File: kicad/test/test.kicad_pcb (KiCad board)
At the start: 2 copper layers, 100.3 x 46.4 mm, 52 parts, among them J1 RJ45, J10 Conn_02x06_Odd_Even, J2 RJ45, J3 Conn_02x06_Odd_Even, J4 Conn_02x06_Odd_Even, J5 Conn_02x06_Odd_Even, J6 Conn_02x06_Odd_Even, J7 Conn_02x06_Odd_Even, J8 Conn_02x06_Odd_Even, J9 Conn_02x06_Odd_Even, U1 SN65LVDS049, U3 TLC5971PWP, U4 MIC5504-3.3YM5

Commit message: V1.0
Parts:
- added J11: Conn_01x02_Pin, Connector_PinSocket_2.54mm:PinSocket_1x02_P2.54mm_Vertical, F.Cu at (154.0, 90.2)
- added R17: 0, Resistor_SMD:R_0805_2012Metric, F.Cu at (154.5, 96.0)
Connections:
- R10 pad 1: +5V -> Net-(J11-Pin_2)
- R11 pad 1: +5V -> Net-(J11-Pin_2)
- R12 pad 1: +5V -> Net-(J11-Pin_2)
- R13 pad 1: +5V -> Net-(J11-Pin_2)
- R14 pad 1: +5V -> Net-(J11-Pin_2)
- R15 pad 1: +5V -> Net-(J11-Pin_2)
- R16 pad 1: +5V -> Net-(J11-Pin_2)
- R5 pad 1: +5V -> Net-(J11-Pin_2)
- R6 pad 1: +5V -> Net-(J11-Pin_2)
- R7 pad 1: +5V -> Net-(J11-Pin_2)
- R8 pad 1: +5V -> Net-(J11-Pin_2)
- R9 pad 1: +5V -> Net-(J11-Pin_2)
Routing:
- net Net-(J11-Pin_2): track 0.00 -> 59.8 mm, vias 0 -> 12
- net +5V: track 28.3 -> 2.89 mm, vias 12 -> 0

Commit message: Cleanup
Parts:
- removed R10, R11, R12, R13, R14, R15, R16, R5, R6, R7, R8, R9: 330, Resistor_SMD:R_0805_2012Metric
- removed U4: MIC5504-3.3YM5, Package_TO_SOT_SMD:SOT-23-5
- moved C3 6.53 mm to (124.2, 95.2), turned to 0 degrees
- moved R17 6.40 mm to (150.5, 91.0), turned to 90 degrees
- moved C2 1.84 mm to (112.0, 95.5)
- moved D10 1.13 mm to (165.1, 91.0)
- moved D11 1.13 mm to (162.6, 91.0)
- moved D12 1.13 mm to (160.0, 91.0)
- moved D13 1.13 mm to (157.5, 91.0)
- moved D2 1.13 mm to (188.0, 91.0)
- moved D3 1.13 mm to (185.4, 91.0)
- moved D4 1.13 mm to (182.9, 91.0)
- moved D5 1.13 mm to (180.3, 91.0)
- moved D6 1.13 mm to (177.8, 91.0)
- moved D7 1.13 mm to (175.3, 91.0)
- moved D8 1.13 mm to (170.2, 91.0)
- moved D9 1.13 mm to (167.6, 91.0)
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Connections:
- C1 pad 1: +5V -> +3V3
- C2 pad 1: +5V -> +3V3
- D11 pad 2: Net-(D11-A) -> Net-(D10-A)
- D12 pad 2: Net-(D12-A) -> Net-(D10-A)
- D13 pad 2: Net-(D13-A) -> Net-(D10-A)
- D2 pad 2: Net-(D2-A) -> Net-(D10-A)
- D3 pad 2: Net-(D3-A) -> Net-(D10-A)
- D4 pad 2: Net-(D4-A) -> Net-(D10-A)
- D5 pad 2: Net-(D5-A) -> Net-(D10-A)
- D6 pad 2: Net-(D6-A) -> Net-(D10-A)
- D7 pad 2: Net-(D7-A) -> Net-(D10-A)
- D8 pad 2: Net-(D8-A) -> Net-(D10-A)
- D9 pad 2: Net-(D9-A) -> Net-(D10-A)
- J1 pad 5: +5V -> +3V3
- J1 pad 7: +5V -> +3V3
- J10 pad 10: +5V -> +3V3
- J10 pad 12: +5V -> +3V3
- J10 pad 2: +5V -> +3V3
- J10 pad 4: +5V -> +3V3
- J10 pad 6: +5V -> +3V3
- J10 pad 8: +5V -> +3V3
- J11 pad 1: +5V -> +3V3
- J11 pad 2: Net-(J11-Pin_2) -> Net-(D10-A)
- J2 pad 5: +5V -> +3V3
- J2 pad 7: +5V -> +3V3
- J3 pad 10: +5V -> +3V3
- J3 pad 12: +5V -> +3V3
- J3 pad 2: +5V -> +3V3
- J3 pad 4: +5V -> +3V3
- J3 pad 6: +5V -> +3V3
- J3 pad 8: +5V -> +3V3
- J4 pad 10: +5V -> +3V3
- J4 pad 12: +5V -> +3V3
- J4 pad 2: +5V -> +3V3
- J4 pad 4: +5V -> +3V3
- J4 pad 6: +5V -> +3V3
- J4 pad 8: +5V -> +3V3
- J5 pad 10: +5V -> +3V3
- J5 pad 12: +5V -> +3V3
- J5 pad 2: +5V -> +3V3
- J5 pad 4: +5V -> +3V3
- J5 pad 6: +5V -> +3V3
- J5 pad 8: +5V -> +3V3
- J6 pad 10: +5V -> +3V3
- J6 pad 12: +5V -> +3V3
- J6 pad 2: +5V -> +3V3
- J6 pad 4: +5V -> +3V3
- J6 pad 6: +5V -> +3V3
- J6 pad 8: +5V -> +3V3
- J7 pad 10: +5V -> +3V3
- J7 pad 12: +5V -> +3V3
- J7 pad 2: +5V -> +3V3
- J7 pad 4: +5V -> +3V3
- J7 pad 6: +5V -> +3V3
- J7 pad 8: +5V -> +3V3
- J8 pad 10: +5V -> +3V3
- J8 pad 12: +5V -> +3V3
- J8 pad 2: +5V -> +3V3
- J8 pad 4: +5V -> +3V3
- J8 pad 6: +5V -> +3V3
- J8 pad 8: +5V -> +3V3
- J9 pad 10: +5V -> +3V3
- J9 pad 12: +5V -> +3V3
- J9 pad 2: +5V -> +3V3
- J9 pad 4: +5V -> +3V3
- J9 pad 6: +5V -> +3V3
- J9 pad 8: +5V -> +3V3
- R17 pad 1: Net-(J11-Pin_2) -> Net-(D10-A)
- R17 pad 2: +5V -> +3V3
- U3 pad 19: +5V -> +3V3
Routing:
- net Net-(J11-Pin_2): track 59.8 -> 0.00 mm, vias 12 -> 0
- net Net-(D10-A): track 2.62 -> 56.9 mm, vias 0 -> 12
- net +3V3: track 18.5 -> 6.42 mm
- net GND: track 42.3 -> 34.4 mm, vias 9 -> 8
- net +5V: track 2.89 -> 0.00 mm
- net Net-(D9-A): track 2.62 -> 0.00 mm
- net Net-(D8-A): track 2.62 -> 0.00 mm
- net Net-(D7-A): track 2.62 -> 0.00 mm
- net Net-(D6-A): track 2.62 -> 0.00 mm
- net Net-(D5-A): track 2.62 -> 0.00 mm
- net Net-(D4-A): track 2.62 -> 0.00 mm
- net Net-(D3-A): track 2.62 -> 0.00 mm
- net Net-(D2-A): track 2.62 -> 0.00 mm
- net Net-(D13-A): track 2.62 -> 0.00 mm
- net Net-(D12-A): track 2.62 -> 0.00 mm
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- removed copper zone on F.Cu, net +5V

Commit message: Fix led driver vcc
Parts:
- added U1: MIC5504-3.3YM5, Package_TO_SOT_SMD:SOT-23-5, F.Cu at (115.5, 94.0)
- moved C1 3.56 mm to (115.2, 97.0), turned to 0 degrees
- moved C2 3.44 mm to (120.8, 95.8), turned to -90 degrees
- renumbered C2 to C1, C3 to C2, C1 to C3, C5 to C4, C6 to C5, C4 to C6, J2 to J1, J8 to J10, J7 to J11, J1 to J2, J11 to J3, J3 to J4, J4 to J5, J5 to J6, J6 to J7, J10 to J8, R2 to R1, R3 to R2, R1 to R3, R17 to R5, U1 to U2
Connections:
- C1 pad 1: +3V3 -> +5V
- J1 pad 5: +3V3 -> +5V
- J1 pad 7: +3V3 -> +5V
- J10 pad 10: +3V3 -> +5V
- J10 pad 12: +3V3 -> +5V
- J10 pad 2: +3V3 -> +5V
- J10 pad 4: +3V3 -> +5V
- J10 pad 6: +3V3 -> +5V
- J10 pad 8: +3V3 -> +5V
- J11 pad 10: +3V3 -> +5V
- J11 pad 12: +3V3 -> +5V
- J11 pad 2: +3V3 -> +5V
- J11 pad 4: +3V3 -> +5V
- J11 pad 6: +3V3 -> +5V
- J11 pad 8: +3V3 -> +5V
- J2 pad 5: +3V3 -> +5V
- J2 pad 7: +3V3 -> +5V
- J3 pad 1: +3V3 -> +5V
- J4 pad 10: +3V3 -> +5V
- J4 pad 12: +3V3 -> +5V
- J4 pad 2: +3V3 -> +5V
- J4 pad 4: +3V3 -> +5V
- J4 pad 6: +3V3 -> +5V
- J4 pad 8: +3V3 -> +5V
- J5 pad 10: +3V3 -> +5V
- J5 pad 12: +3V3 -> +5V
- J5 pad 2: +3V3 -> +5V
- J5 pad 4: +3V3 -> +5V
- J5 pad 6: +3V3 -> +5V
- J5 pad 8: +3V3 -> +5V
- J6 pad 10: +3V3 -> +5V
- J6 pad 12: +3V3 -> +5V
- J6 pad 2: +3V3 -> +5V
- J6 pad 4: +3V3 -> +5V
- J6 pad 6: +3V3 -> +5V
- J6 pad 8: +3V3 -> +5V
- J7 pad 10: +3V3 -> +5V
- J7 pad 12: +3V3 -> +5V
- J7 pad 2: +3V3 -> +5V
- J7 pad 4: +3V3 -> +5V
- J7 pad 6: +3V3 -> +5V
- J7 pad 8: +3V3 -> +5V
- J8 pad 10: +3V3 -> +5V
- J8 pad 12: +3V3 -> +5V
- J8 pad 2: +3V3 -> +5V
- J8 pad 4: +3V3 -> +5V
- J8 pad 6: +3V3 -> +5V
- J8 pad 8: +3V3 -> +5V
- J9 pad 10: +3V3 -> +5V
- J9 pad 12: +3V3 -> +5V
- J9 pad 2: +3V3 -> +5V
- J9 pad 4: +3V3 -> +5V
- J9 pad 6: +3V3 -> +5V
- J9 pad 8: +3V3 -> +5V
- R3 pad 1: +3V3 -> +5V
- R5 pad 2: +3V3 -> +5V
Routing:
- net GND: track 34.4 -> 34.8 mm, vias 8 -> 11
- added copper zone on F.Cu, net +5V
- added copper zone on F.Cu, net GND

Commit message: cleanup
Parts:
- moved C1 4.28 mm to (114.8, 92.8)
- moved U1 1.75 mm to (115.5, 95.8)
- moved C2 0.25 mm to (120.5, 95.8)
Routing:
- net GND: track 34.8 -> 28.8 mm, vias 11 -> 13
- net Net-(D8-K): track 120.4 -> 119.4 mm

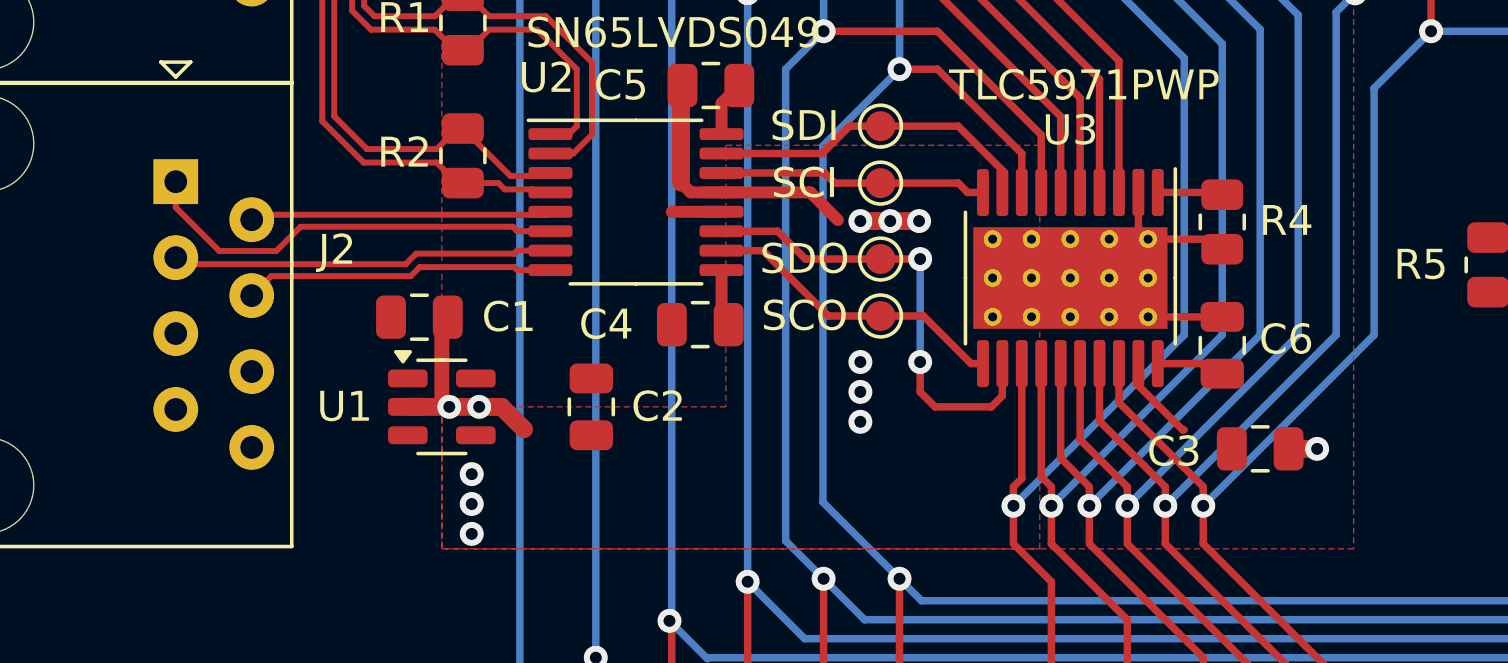
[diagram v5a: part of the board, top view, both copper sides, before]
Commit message: fix vreg on led driver
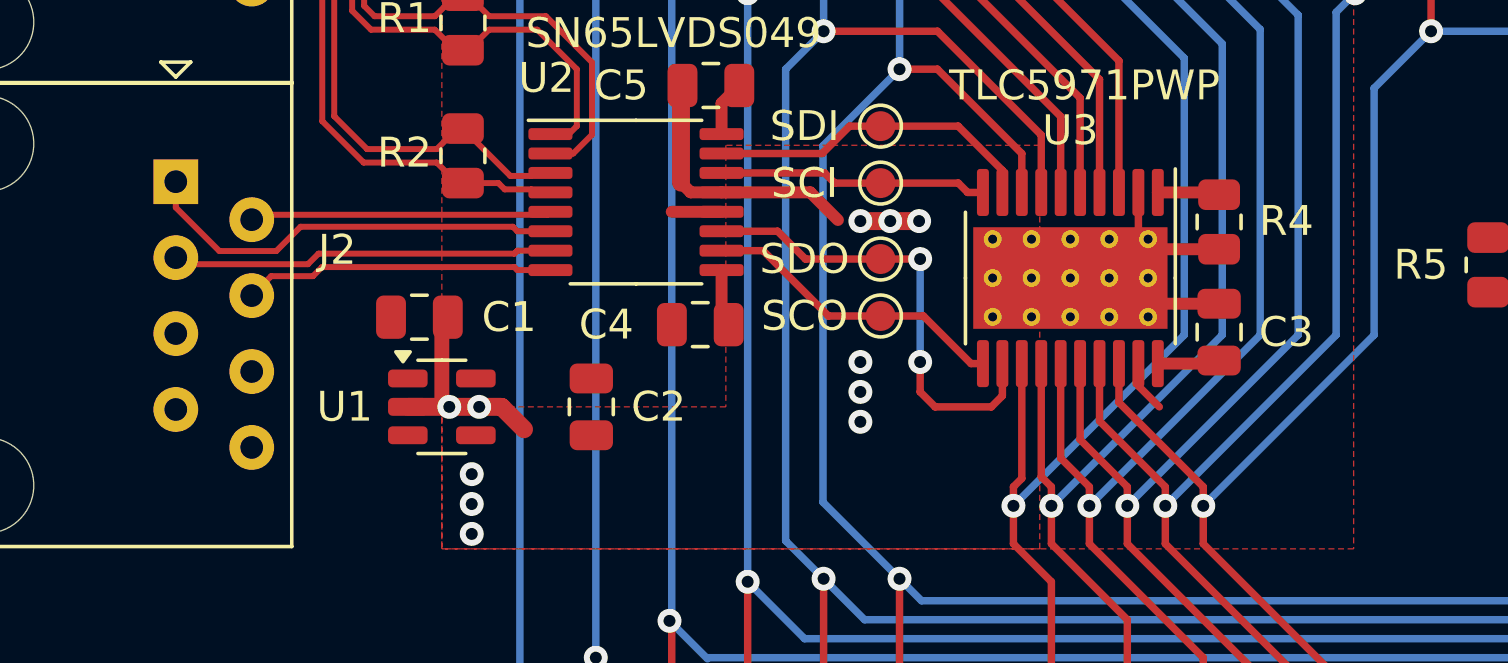
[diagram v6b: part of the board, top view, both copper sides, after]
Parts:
- removed C6: 1uF, Capacitor_SMD:C_0805_2012Metric
- moved C3 4.14 mm to (141.5, 93.2), turned to 90 degrees
- moved R4 0.10 mm to (141.5, 89.6)
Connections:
- U3 pad 20: Net-(U3-VREG) -> +3V3
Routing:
- net Net-(U3-VREG): track 2.29 -> 0.00 mm
- net +3V3: track 6.42 -> 7.37 mm
- net GND: track 28.8 -> 28.4 mm, vias 13 -> 12

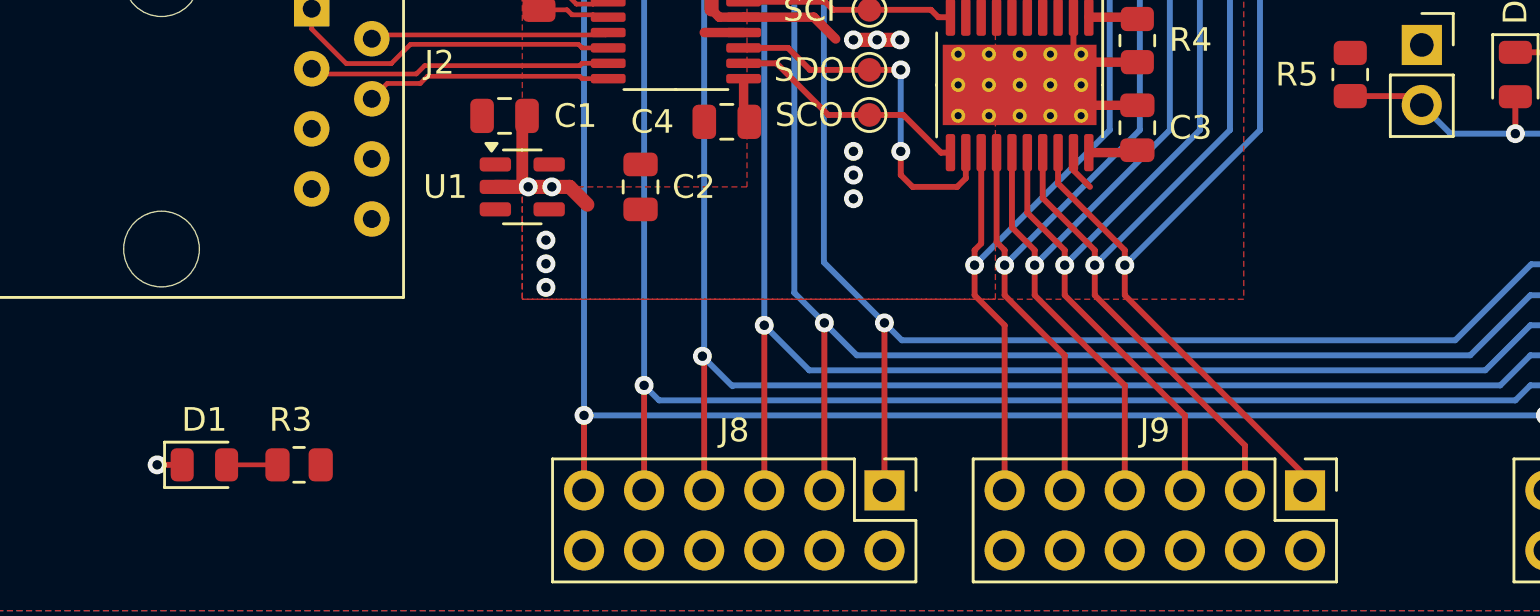
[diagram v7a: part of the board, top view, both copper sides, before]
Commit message: Add power test points
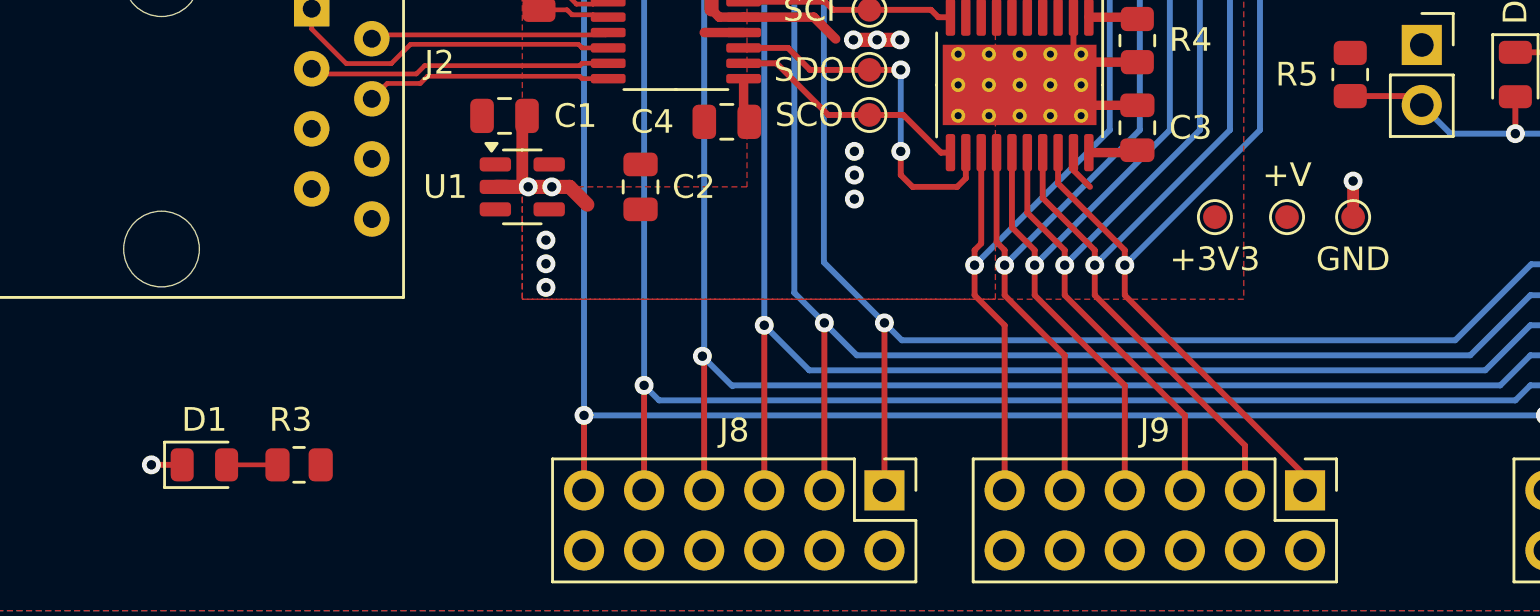
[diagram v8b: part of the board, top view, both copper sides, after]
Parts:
- added +3V3: TestPoint_Pad_D1.0mm, TestPoint:TestPoint_Pad_D1.0mm, F.Cu at (144.8, 97.0)
- added +V: TestPoint_Pad_D1.0mm, TestPoint:TestPoint_Pad_D1.0mm, F.Cu at (147.8, 97.0)
- added GND: TestPoint_Pad_D1.0mm, TestPoint:TestPoint_Pad_D1.0mm, F.Cu at (150.6, 97.0)
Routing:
- net GND: track 28.4 -> 30.2 mm, vias 12 -> 13
